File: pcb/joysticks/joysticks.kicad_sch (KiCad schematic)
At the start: 6 parts, among them J1001 Conn_01x01_Socket, J1007 Conn_01x01_Socket

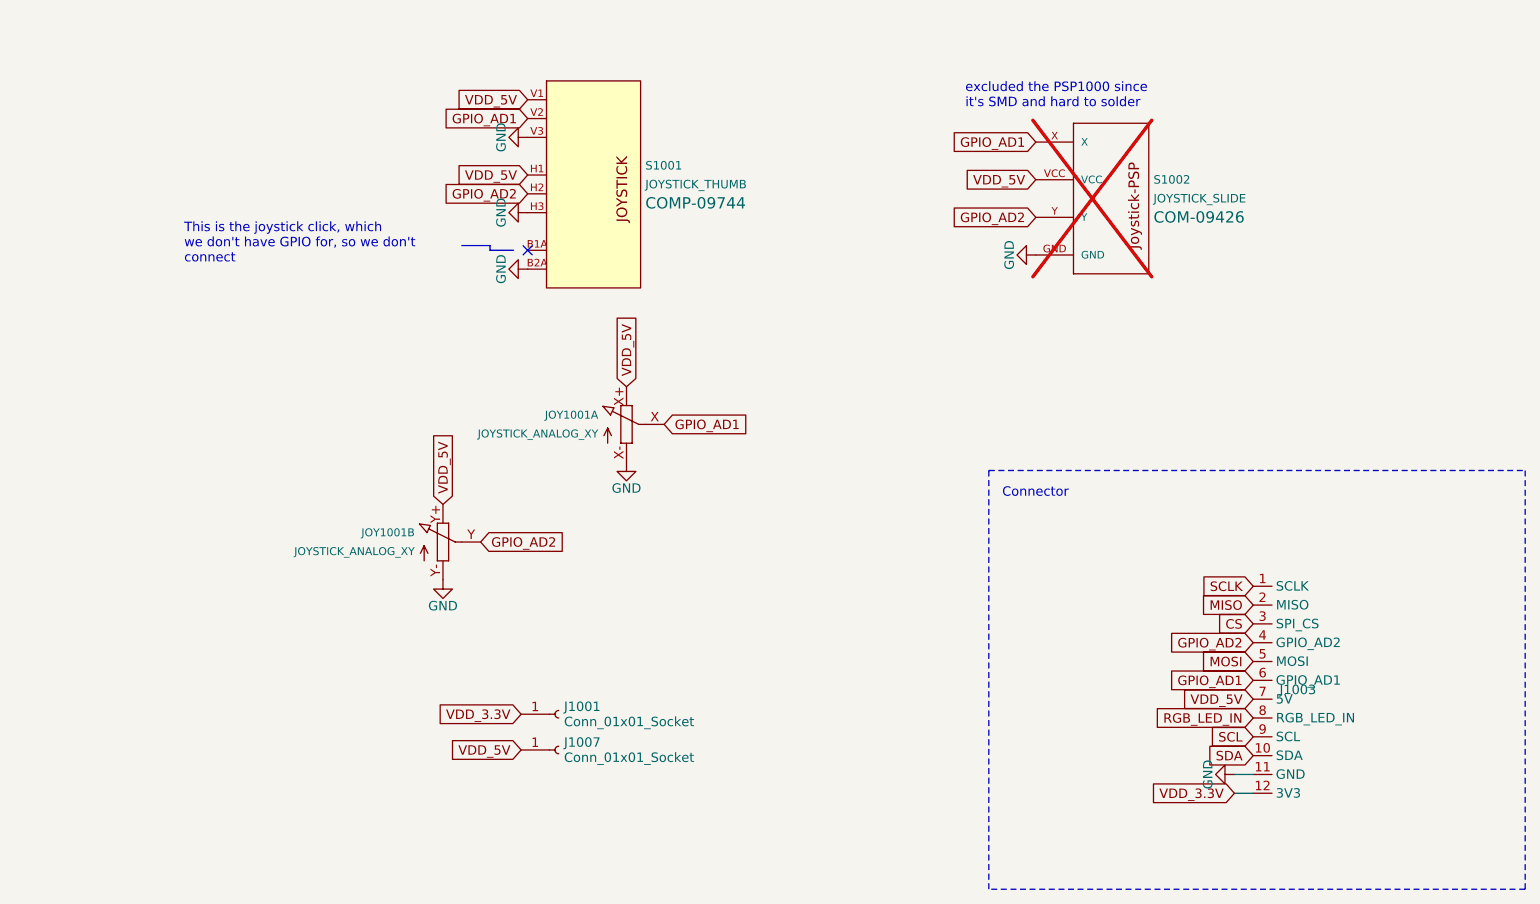
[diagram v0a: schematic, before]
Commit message: added joycon connector to joysticks module
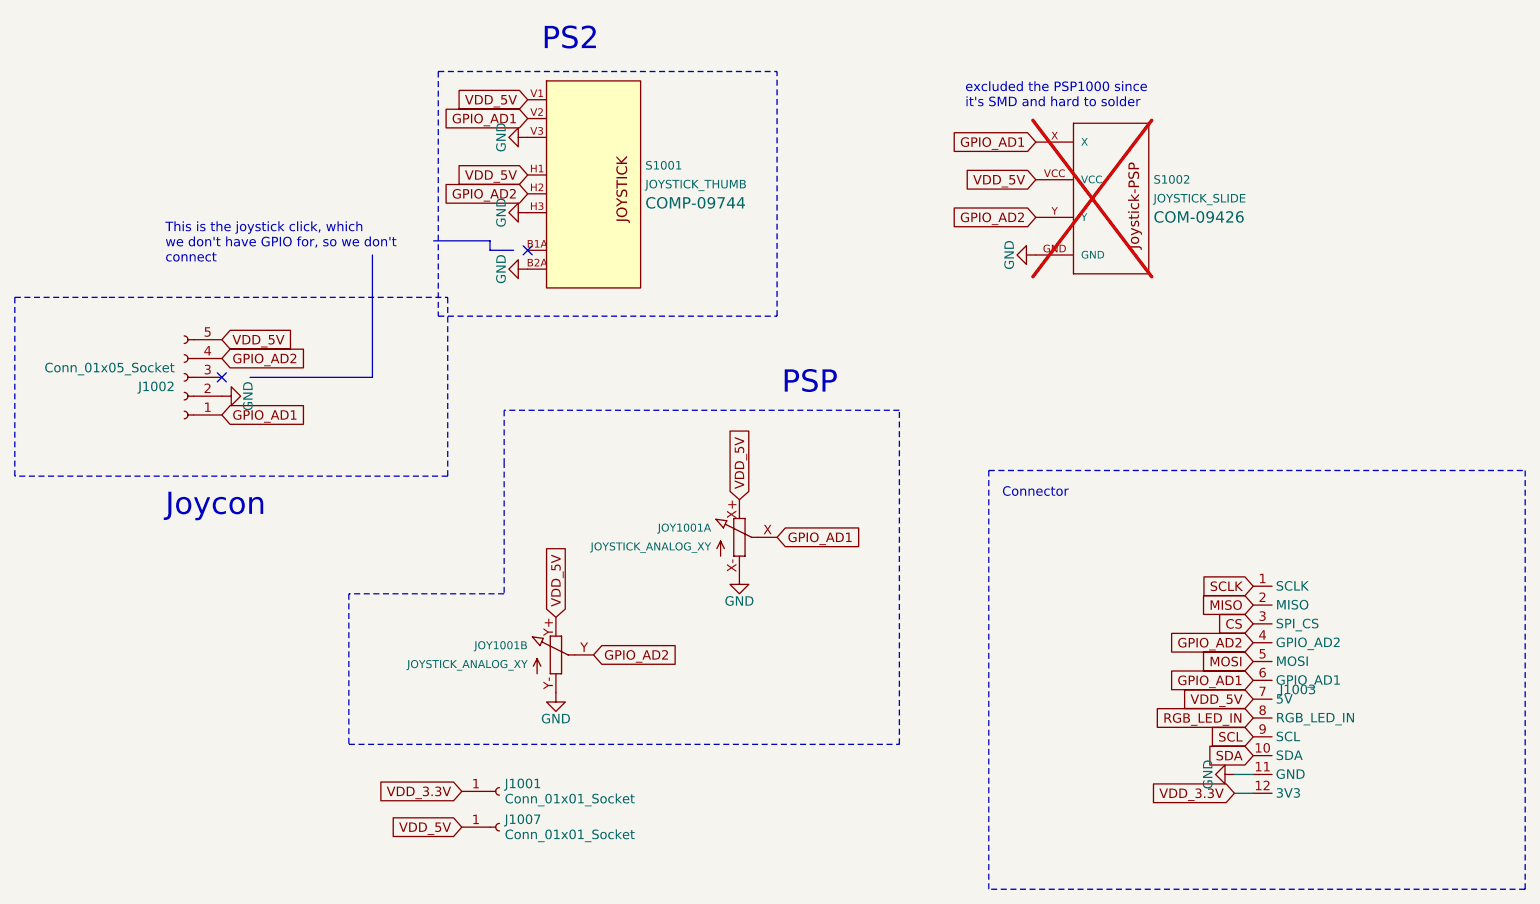
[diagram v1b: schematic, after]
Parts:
- added J1002: Conn_01x05_Socket, Connector_FFC-FPC:TE_0-1734839-5_1x05-1MP_P0.5mm_Horizontal, symbol Connector:Conn_01x05_Socket
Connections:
- net GND: now also J1002.2 (Pin_2)
- net GPIO_AD1: now also J1002.1 (Pin_1)
- net GPIO_AD2: now also J1002.4 (Pin_4)
- net VDD_5V: now also J1002.5 (Pin_5)
- no-connect marks 1 -> 2
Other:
- note added: "Joycon"
- note added: "PS2"
- note added: "PSP"
- moved on the sheet: J1001, J1007, JOY1001A, JOY1001B

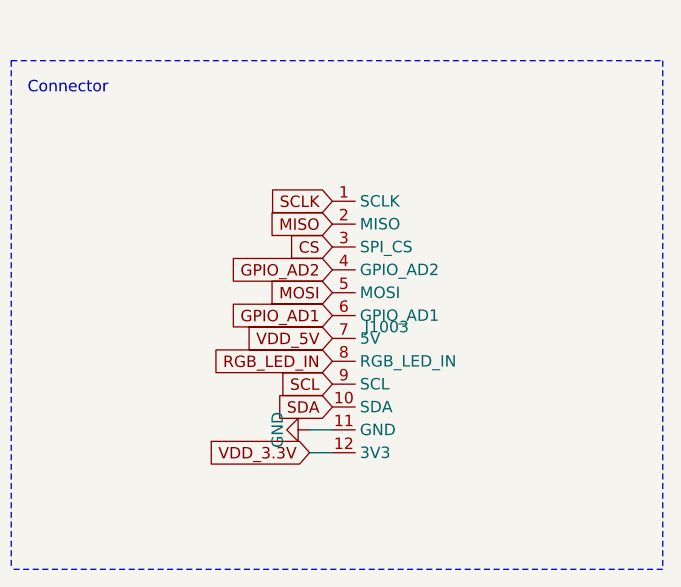
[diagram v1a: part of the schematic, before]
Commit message: updated vikm connector symbols, per some recommendations from sigprof in fingerpunch discord
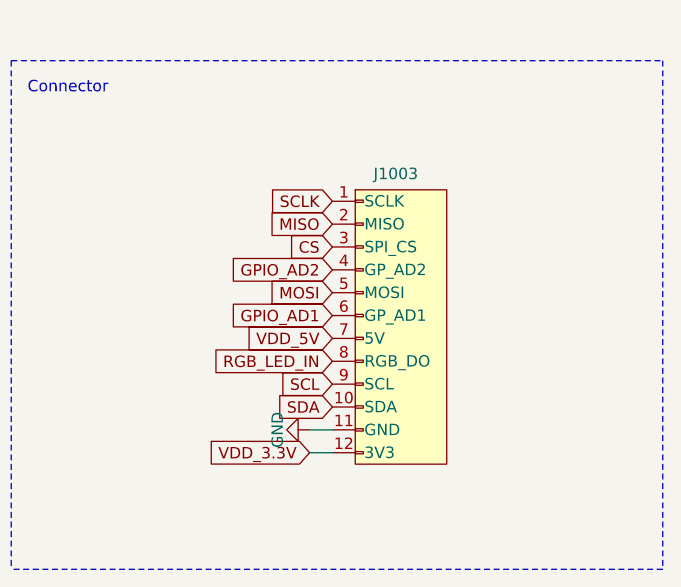
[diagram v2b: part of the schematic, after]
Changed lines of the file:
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@@
     )
   )
-  (symbol (lib_id "vik:vik-module-connector") (at 186.182 132.334 0) (unit 1)
-    (in_bom yes) (on_board yes) (dnp no) (fields_autoplaced)
-    (property "Reference" "J1003" (at 189.738 132.334 0)
+  (symbol (lib_id "vik:vik-module-connector") (at 193.802 131.064 0) (unit 1)
+    (in_bom yes) (on_board yes) (dnp no)
+    (property "Reference" "J1003" (at 190.754 115.316 0)
       (effects (font (size 1.27 1.27)) (justify left))
     )
-    (property "Value" "~" (at 186.182 125.984 0)
+    (property "Value" "~" (at 193.802 124.714 0)
       (effects (font (size 1.27 1.27)))
     )
-    (property "Footprint" "vik:vik-module-connector-horizontal" (at 186.182 125.984 0)
+    (property "Footprint" "vik:vik-module-connector-horizontal" (at 193.802 124.714 0)
       (effects (font (size 1.27 1.27)) hide)
     )
-    (property "Datasheet" "" (at 186.182 125.984 0)
+    (property "Datasheet" "" (at 193.802 124.714 0)
       (effects (font (size 1.27 1.27)) hide)
     )
-    (property "LCSC" "C2919557" (at 186.182 132.334 0)
+    (property "LCSC" "C2919557" (at 193.802 131.064 0)
       (effects (font (size 1.27 1.27)) hide)
     )

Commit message: incorrect copyright messages in some of the schema files
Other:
- company: bastard keyboards -> (none)
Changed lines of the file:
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@@
   (paper "A4")
   (title_block
-    (company "bastard keyboards")
-    (comment 4 "Copyright Quentin Lebastard")
+    (comment 4 "https://github.com/sadekbaroudi/vik")
   )
   (no_connect (at 88.265 73.025))
